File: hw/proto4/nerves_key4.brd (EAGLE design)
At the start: 8.9 x 13.2 mm, 3 parts, among them U1 ATECC508A-SSHDA

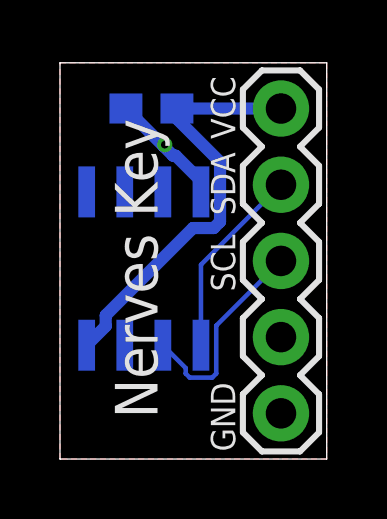
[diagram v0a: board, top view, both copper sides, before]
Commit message: Save 5 cents
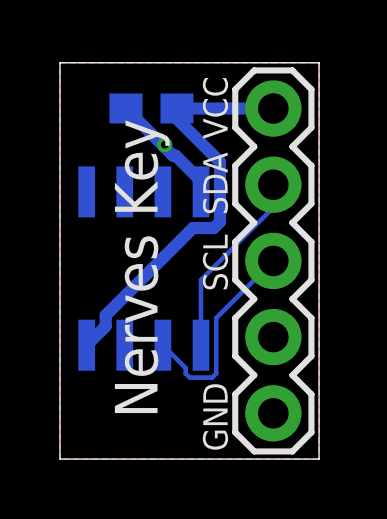
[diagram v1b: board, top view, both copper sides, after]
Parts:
- moved J1 0.25 mm to (7.11, 11.7)
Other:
- board size 8.9 x 13.2 mm -> 8.6 x 13.2 mm
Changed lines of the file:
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@@
 <board>
 <plain>
-<wire x1="0" y1="0" x2="8.89" y2="0" width="0" layer="20"/>
-<wire x1="8.89" y1="0" x2="8.89" y2="13.208" width="0" layer="20"/>
-<wire x1="8.89" y1="13.208" x2="0" y2="13.208" width="0" layer="20"/>
+<wire x1="0" y1="0" x2="8.636" y2="0" width="0" layer="20"/>
+<wire x1="8.636" y1="0" x2="8.636" y2="13.208" width="0" layer="20"/>
+<wire x1="8.636" y1="13.208" x2="0" y2="13.208" width="0" layer="20"/>
 <wire x1="0" y1="13.208" x2="0" y2="0" width="0" layer="20"/>
 <text x="2.54" y="6.35" size="1.4224" layer="25" rot="SR90" align="center">Nerves Key</text>
-<text x="5.842" y="10.668" size="0.8128" layer="25" rot="R90">VCC</text>
-<text x="5.842" y="8.128" size="0.8128" layer="25" rot="R90">SDA</text>
-<text x="5.842" y="5.588" size="0.8128" layer="25" rot="R90">SCL</text>
-<text x="5.842" y="0.254" size="0.8128" layer="25" rot="R90">GND</text>
+<text x="5.588" y="10.668" size="0.8128" layer="25" rot="R90">VCC</text>
+<text x="5.588" y="8.128" size="0.8128" layer="25" rot="R90">SDA</text>
+<text x="5.588" y="5.588" size="0.8128" layer="25" rot="R90">SCL</text>
+<text x="5.588" y="0.254" size="0.8128" layer="25" rot="R90">GND</text>
 </plain>
 <attributes>
@@
 </element>
 <element name="U1" library="cryptopi" package="SOIC127P625X175-8" package3d_urn="urn:adsk.eagle:package:4514464/1" value="ATECC508A-SSHDA" x="2.794" y="6.35" smashed="yes" rot="MR270"/>
-<element name="J1" library="SparkFun-Connectors" library_urn="urn:adsk.eagle:library:513" package="1X05" package3d_urn="urn:adsk.eagle:package:38104/1" value="" x="7.366" y="11.684" smashed="yes" rot="R270">
-<attribute name="VALUE" x="5.334" y="12.954" size="0.6096" layer="27" font="vector" ratio="20" rot="R270"/>
+<element name="J1" library="SparkFun-Connectors" library_urn="urn:adsk.eagle:library:513" package="1X05" package3d_urn="urn:adsk.eagle:package:38104/1" value="" x="7.112" y="11.684" smashed="yes" rot="R270">
+<attribute name="VALUE" x="5.08" y="12.954" size="0.6096" layer="27" font="vector" ratio="20" rot="R270"/>
 </element>
 </elements>
@@
 <contactref element="C1" pad="1"/>
 <contactref element="J1" pad="1"/>
-<wire x1="7.366" y1="11.684" x2="3.898" y2="11.684" width="0.4064" layer="16"/>
+<wire x1="7.112" y1="11.684" x2="3.898" y2="11.684" width="0.4064" layer="16"/>
 <wire x1="0.889" y1="3.7941" x2="1.52385" y2="4.42895" width="0.4064" layer="16"/>
 <wire x1="1.52385" y1="4.42895" x2="1.52385" y2="4.79164375" width="0.4064" layer="16"/>
@@
 <contactref element="U1" pad="6"/>
 <contactref element="J1" pad="3"/>
-<wire x1="7.366" y1="6.604" x2="5.20715" y2="4.44515" width="0.1524" layer="16"/>
-<wire x1="5.20715" y1="4.44515" x2="5.20715" y2="2.8491625" width="0.1524" layer="16"/>
+<wire x1="7.112" y1="6.604" x2="5.20715" y2="4.69915" width="0.1524" layer="16"/>
+<wire x1="5.20715" y1="4.69915" x2="5.20715" y2="2.8491625" width="0.1524" layer="16"/>
 <wire x1="5.20715" y1="2.8491625" x2="5.0732375" y2="2.71525" width="0.1524" layer="16"/>
 <wire x1="5.0732375" y1="2.71525" x2="4.3247625" y2="2.71525" width="0.1524" layer="16"/>
@@
 <contactref element="U1" pad="5"/>
 <contactref element="J1" pad="2"/>
-<wire x1="7.366" y1="9.144" x2="4.699" y2="6.477" width="0.1524" layer="16"/>
-<wire x1="4.699" y1="6.477" x2="4.699" y2="3.7941" width="0.1524" layer="16"/>
+<wire x1="4.699" y1="3.7941" x2="4.699" y2="5.969" width="0.1524" layer="16"/>
+<wire x1="4.699" y1="5.969" x2="7.112" y2="8.382" width="0.1524" layer="16"/>
+<wire x1="7.112" y1="8.382" x2="7.112" y2="9.144" width="0.1524" layer="16"/>
 </signal>
 <signal name="GND">
@@
 <polygon width="0.4064" layer="1">
 <vertex x="0" y="13.208"/>
-<vertex x="8.89" y="13.208"/>
-<vertex x="8.89" y="0"/>
+<vertex x="8.636" y="13.208"/>
+<vertex x="8.636" y="0"/>
 <vertex x="0" y="0"/>
 </polygon>

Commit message: Fix ERC/DRC
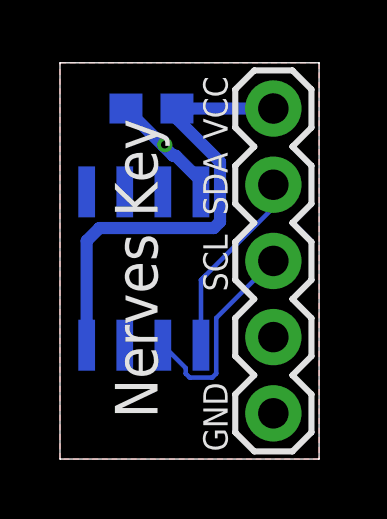
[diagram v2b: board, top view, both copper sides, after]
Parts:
- J1: value (none) -> RPI_GPIO
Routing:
- net VCC: track 13.9 -> 15.8 mm
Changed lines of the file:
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@@
 </element>
 <element name="U1" library="cryptopi" package="SOIC127P625X175-8" package3d_urn="urn:adsk.eagle:package:4514464/1" value="ATECC508A-SSHDA" x="2.794" y="6.35" smashed="yes" rot="MR270"/>
-<element name="J1" library="SparkFun-Connectors" library_urn="urn:adsk.eagle:library:513" package="1X05" package3d_urn="urn:adsk.eagle:package:38104/1" value="" x="7.112" y="11.684" smashed="yes" rot="R270">
+<element name="J1" library="SparkFun-Connectors" library_urn="urn:adsk.eagle:library:513" package="1X05" package3d_urn="urn:adsk.eagle:package:38104/1" value="RPI_GPIO" x="7.112" y="11.684" smashed="yes" rot="R270">
 <attribute name="VALUE" x="5.08" y="12.954" size="0.6096" layer="27" font="vector" ratio="20" rot="R270"/>
 </element>
@@
 <signals>
 <signal name="VCC">
+<contactref element="J1" pad="1"/>
 <contactref element="U1" pad="8"/>
 <contactref element="C1" pad="1"/>
-<contactref element="J1" pad="1"/>
 <wire x1="7.112" y1="11.684" x2="3.898" y2="11.684" width="0.4064" layer="16"/>
-<wire x1="0.889" y1="3.7941" x2="1.52385" y2="4.42895" width="0.4064" layer="16"/>
-<wire x1="1.52385" y1="4.42895" x2="1.52385" y2="4.79164375" width="0.4064" layer="16"/>
-<wire x1="5.12584375" y1="7.70005" x2="5.33415" y2="7.90835625" width="0.4064" layer="16"/>
-<wire x1="5.33415" y1="7.90835625" x2="5.33415" y2="9.90344375" width="0.4064" layer="16"/>
-<wire x1="4.43225625" y1="7.70005" x2="5.12584375" y2="7.70005" width="0.4064" layer="16"/>
-<wire x1="3.898" y1="11.33959375" x2="3.898" y2="11.684" width="0.4064" layer="16"/>
-<wire x1="1.52385" y1="4.79164375" x2="4.43225625" y2="7.70005" width="0.4064" layer="16"/>
-<wire x1="5.33415" y1="9.90344375" x2="3.898" y2="11.33959375" width="0.4064" layer="16"/>
-</signal>
-<signal name="SCL">
-<contactref element="U1" pad="6"/>
-<contactref element="J1" pad="3"/>
-<wire x1="7.112" y1="6.604" x2="5.20715" y2="4.69915" width="0.1524" layer="16"/>
-<wire x1="5.20715" y1="4.69915" x2="5.20715" y2="2.8491625" width="0.1524" layer="16"/>
-<wire x1="5.20715" y1="2.8491625" x2="5.0732375" y2="2.71525" width="0.1524" layer="16"/>
-<wire x1="5.0732375" y1="2.71525" x2="4.3247625" y2="2.71525" width="0.1524" layer="16"/>
-<wire x1="4.3247625" y1="2.71525" x2="4.19085" y2="2.8491625" width="0.1524" layer="16"/>
-<wire x1="4.19085" y1="2.8491625" x2="4.19085" y2="3.03225" width="0.1524" layer="16"/>
-<wire x1="4.19085" y1="3.03225" x2="3.429" y2="3.7941" width="0.1524" layer="16"/>
+<wire x1="5.33415" y1="9.90344375" x2="5.33415" y2="7.90835625" width="0.4064" layer="16"/>
+<wire x1="5.33415" y1="7.90835625" x2="5.12584375" y2="7.70005" width="0.4064" layer="16"/>
+<wire x1="1.31584375" y1="7.70005" x2="0.889" y2="7.27320625" width="0.4064" layer="16"/>
+<wire x1="0.889" y1="7.27320625" x2="0.889" y2="3.7941" width="0.4064" layer="16"/>
+<wire x1="5.12584375" y1="7.70005" x2="1.31584375" y2="7.70005" width="0.4064" layer="16"/>
+<wire x1="3.898" y1="11.684" x2="3.898" y2="11.33959375" width="0.4064" layer="16"/>
+<wire x1="3.898" y1="11.33959375" x2="5.33415" y2="9.90344375" width="0.4064" layer="16"/>
 </signal>
 <signal name="SDA">
+<contactref element="J1" pad="2"/>
+<wire x1="4.699" y1="5.969" x2="4.826" y2="6.096" width="0.1524" layer="16"/>
+<wire x1="4.826" y1="6.096" x2="7.112" y2="8.382" width="0.1524" layer="16"/>
+<wire x1="7.112" y1="8.382" x2="7.112" y2="9.144" width="0.1524" layer="16"/>
 <contactref element="U1" pad="5"/>
-<contactref element="J1" pad="2"/>
-<wire x1="4.699" y1="3.7941" x2="4.699" y2="5.969" width="0.1524" layer="16"/>
-<wire x1="4.699" y1="5.969" x2="7.112" y2="8.382" width="0.1524" layer="16"/>
-<wire x1="7.112" y1="8.382" x2="7.112" y2="9.144" width="0.1524" layer="16"/>
+<wire x1="4.826" y1="6.096" x2="4.699" y2="5.969" width="0.1524" layer="16"/>
+<wire x1="4.699" y1="5.969" x2="4.699" y2="3.7941" width="0.1524" layer="16"/>
 </signal>
 <signal name="GND">
@@
 <via x="3.4925" y="10.4775" extent="1-16" drill="0.254"/>
 </signal>
+<signal name="SCL">
+<contactref element="U1" pad="6"/>
+<contactref element="J1" pad="3"/>
+<wire x1="7.112" y1="6.604" x2="5.20715" y2="4.69915" width="0.1524" layer="16"/>
+<wire x1="5.20715" y1="4.69915" x2="5.20715" y2="2.8491625" width="0.1524" layer="16"/>
+<wire x1="5.20715" y1="2.8491625" x2="5.0732375" y2="2.71525" width="0.1524" layer="16"/>
+<wire x1="5.0732375" y1="2.71525" x2="4.3247625" y2="2.71525" width="0.1524" layer="16"/>
+<wire x1="4.3247625" y1="2.71525" x2="4.19085" y2="2.8491625" width="0.1524" layer="16"/>
+<wire x1="4.19085" y1="2.8491625" x2="4.19085" y2="3.03225" width="0.1524" layer="16"/>
+<wire x1="4.19085" y1="3.03225" x2="3.429" y2="3.7941" width="0.1524" layer="16"/>
+</signal>
 </signals>
